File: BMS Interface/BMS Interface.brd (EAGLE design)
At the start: 55.2 x 82.9 mm, 23 parts

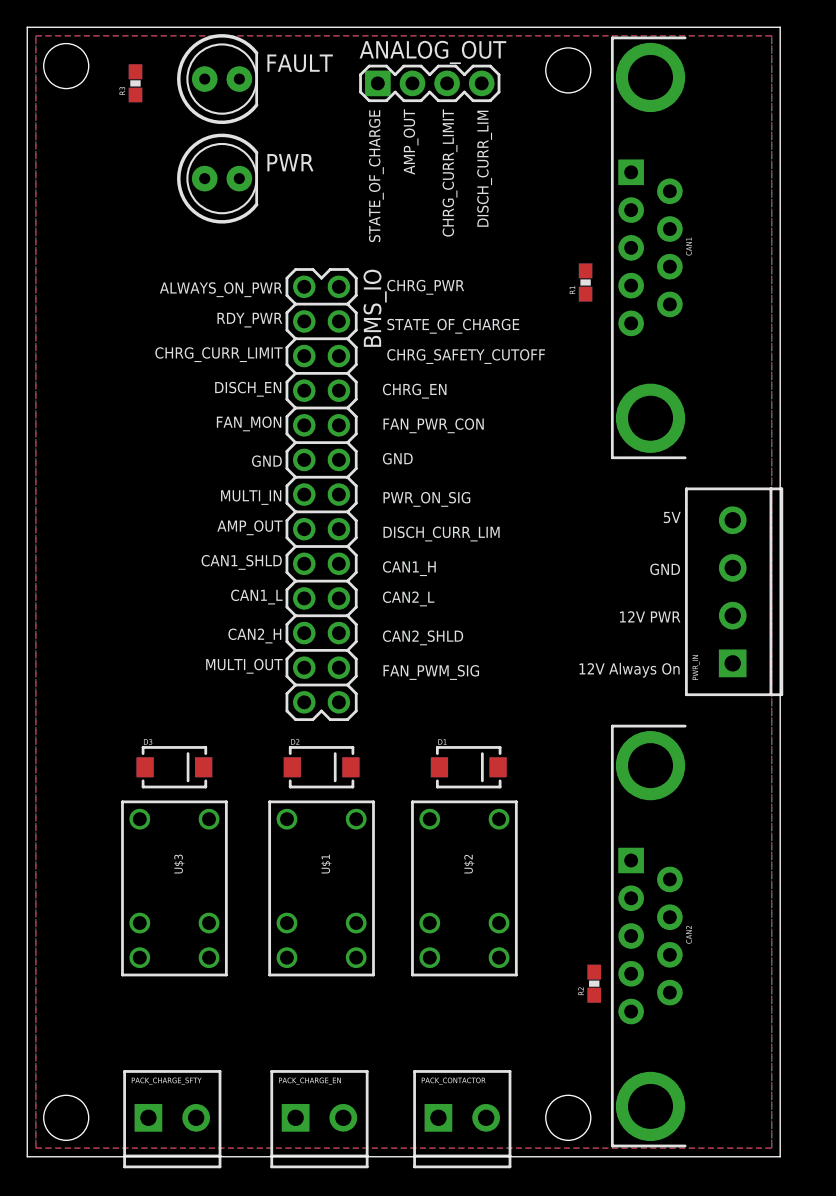
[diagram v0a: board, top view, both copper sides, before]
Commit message: Updating layout for BMS interface PCB and removed 5V input as it was no longer necessary.
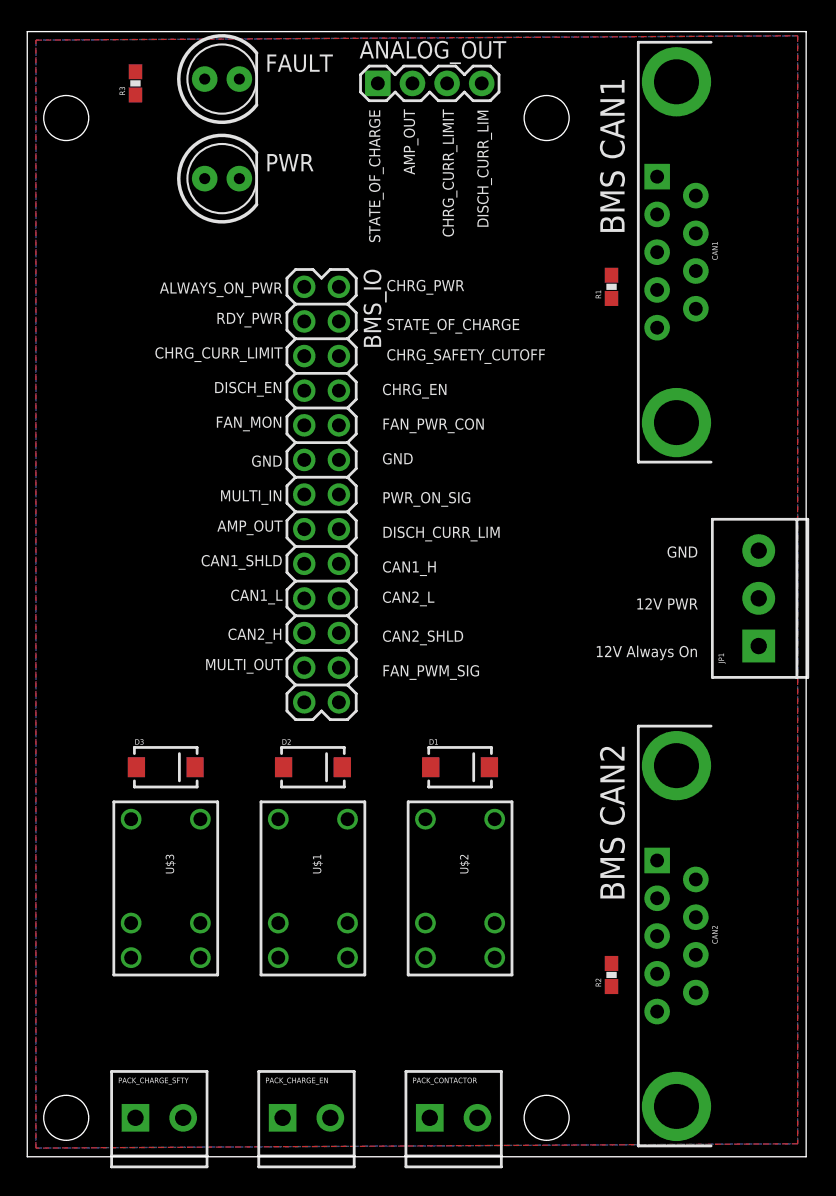
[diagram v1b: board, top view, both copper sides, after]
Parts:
- removed PWR_IN: (no value), SparkFun-Connectors:SCREWTERMINAL-3.5MM-4
- added JP1: (no value), SparkFun-Connectors:SCREWTERMINAL-3.5MM-3
- moved STANDOFF4 3.84 mm to (38.1, 76.2)
- moved STANDOFF2 3.81 mm to (2.86, 76.2)
- moved CAN1 1.93 mm to (47.6, 66.4)
- moved R1 1.93 mm to (42.9, 63.8)
- moved CAN2 1.91 mm to (47.6, 16.2)
- moved STANDOFF3 1.59 mm to (38.1, 2.86)
- moved R2 1.42 mm to (42.9, 13.3)
- moved PACK_CHARGE_SFTY 0.95 mm to (7.94, 2.86)
- moved PACK_CHARGE_EN 0.95 mm to (18.7, 2.86)
- moved D2 0.64 mm to (21.0, 28.6)
- moved PACK_CONTACTOR 0.64 mm to (29.5, 2.86)
- moved U$1 0.64 mm to (21.0, 19.7)
- moved D3 0.63 mm to (10.2, 28.6)
- moved U$3 0.63 mm to (10.2, 19.7)
- moved D1 0.63 mm to (31.8, 28.6)
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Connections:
- removed net 5V: PWR_IN.4
- net 12V_PWR: now also JP1.2; no longer PWR_IN.2
- net ALWAYS_ON_PWR: now also JP1.1; no longer PWR_IN.1
- net GND: now also JP1.3; no longer PWR_IN.3
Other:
- board size 55.2 x 82.9 mm -> 57.1 x 82.5 mm
- board text added: "BMS CAN1"
- board text added: "BMS CAN2"
- board text removed: "5V"

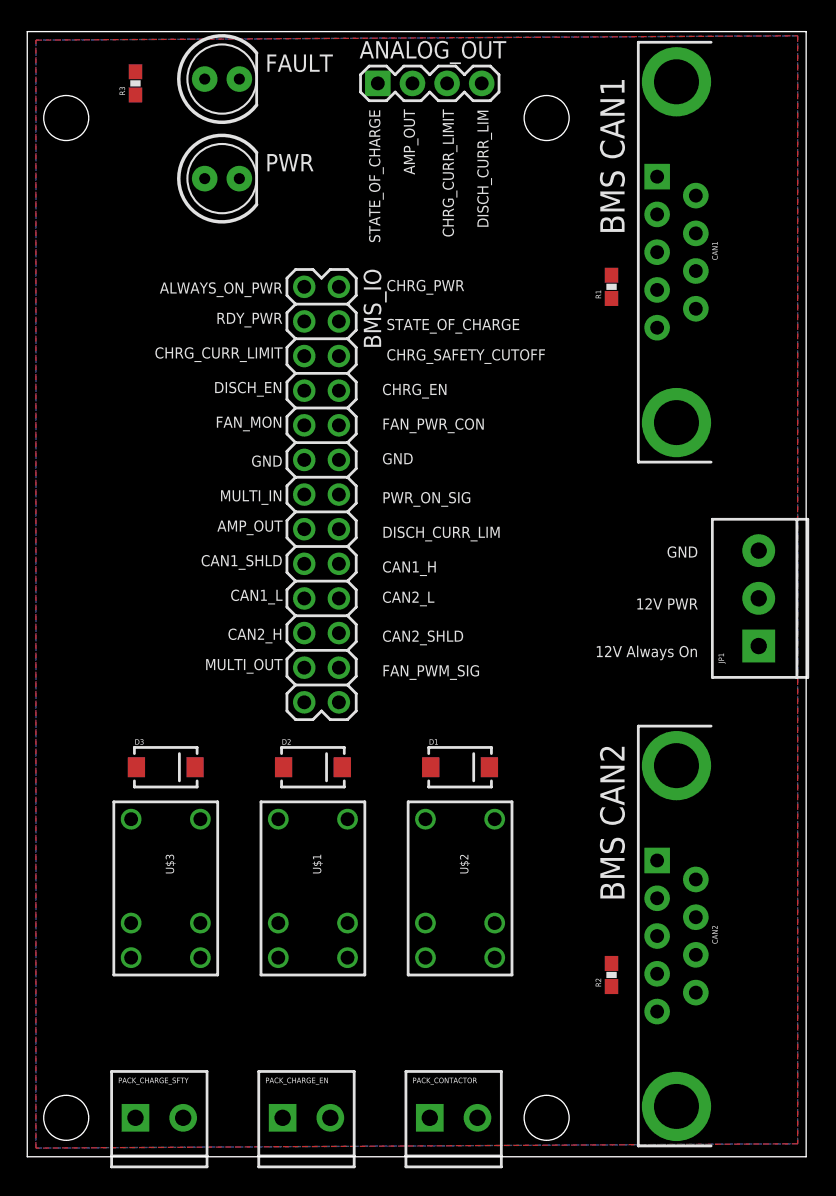
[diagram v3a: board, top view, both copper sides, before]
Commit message: CHanged all connectors on MCB to use Molex
Changed most of the connectors on the BMS interface to use molex as
well.
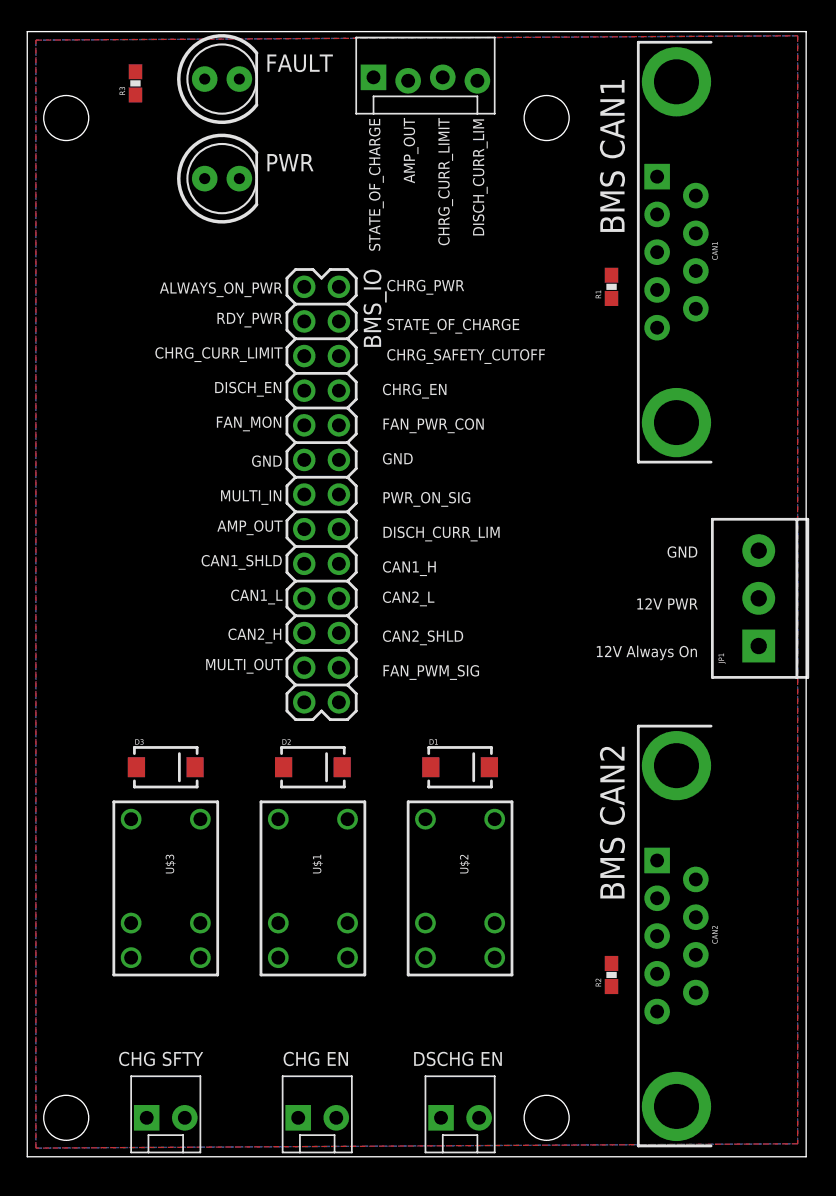
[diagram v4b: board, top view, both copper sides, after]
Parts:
- ANALOG_OUT: device SparkFun-Connectors:1X04 -> SparkFun-Connectors:MOLEX-1X4_LOCK
- PACK_CHARGE_EN, PACK_CHARGE_SFTY, PACK_CONTACTOR: value M023.5MM -> M02POLAR_LOCK; device SparkFun-Connectors:SCREWTERMINAL-3.5MM-2 -> SparkFun-Connectors:MOLEX-1X2_LOCK
- moved PACK_CHARGE_EN 1.27 mm to (20.0, 2.86)
- moved PACK_CHARGE_SFTY 0.95 mm to (8.89, 2.86)
- moved PACK_CONTACTOR 0.95 mm to (30.5, 2.86)
- moved ANALOG_OUT 0.45 mm to (25.4, 79.1)
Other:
- board text added: "CHG EN"
- board text added: "CHG SFTY"
- board text added: "DSCHG EN"
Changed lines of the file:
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@@
 <text x="49.2125" y="40.9575" size="0.8128" layer="25" font="vector" ratio="15" rot="R180">12V PWR</text>
 <text x="49.2125" y="44.7675" size="0.8128" layer="25" font="vector" ratio="15" rot="R180">GND</text>
-<text x="33.02" y="76.835" size="0.8128" layer="25" font="vector" ratio="15" rot="R270">DISCH_CURR_LIM</text>
-<text x="30.48" y="76.835" size="0.8128" layer="25" font="vector" ratio="15" rot="R270">CHRG_CURR_LIMIT</text>
-<text x="27.6225" y="76.835" size="0.8128" layer="25" font="vector" ratio="15" rot="R270">AMP_OUT</text>
-<text x="25.0825" y="76.835" size="0.8128" layer="25" font="vector" ratio="15" rot="R270">STATE_OF_CHARGE</text>
+<text x="32.7025" y="76.2" size="0.8128" layer="25" font="vector" ratio="15" rot="R270">DISCH_CURR_LIM</text>
+<text x="30.1625" y="76.2" size="0.8128" layer="25" font="vector" ratio="15" rot="R270">CHRG_CURR_LIMIT</text>
+<text x="27.6225" y="76.2" size="0.8128" layer="25" font="vector" ratio="15" rot="R270">AMP_OUT</text>
+<text x="25.0825" y="76.2" size="0.8128" layer="25" font="vector" ratio="15" rot="R270">STATE_OF_CHARGE</text>
 <text x="43.815" y="67.6275" size="1.778" layer="25" font="vector" ratio="15" rot="R90">BMS CAN1</text>
 <text x="43.815" y="18.7325" size="1.778" layer="25" font="vector" ratio="15" rot="R90">BMS CAN2</text>
+<text x="6.6675" y="6.6675" size="1.016" layer="25" font="vector" ratio="15">CHG SFTY</text>
+<text x="18.7325" y="6.6675" size="1.016" layer="25" font="vector" ratio="15">CHG EN</text>
+<text x="28.2575" y="6.6675" size="1.016" layer="25" font="vector" ratio="15">DSCHG EN</text>
 </plain>
 <attributes>
@@
 <element name="U$1" library="SparkFun-Electromechanical" package="RELAY-G5V" value="RELAY-2G5Q" x="20.955" y="19.685" rot="R270"/>
 <element name="U$2" library="SparkFun-Electromechanical" package="RELAY-G5V" value="RELAY-2G5Q" x="31.75" y="19.685" rot="R270"/>
-<element name="PACK_CONTACTOR" library="SparkFun-Connectors" package="SCREWTERMINAL-3.5MM-2" value="M023.5MM" x="29.5275" y="2.8575"/>
 <element name="D1" library="SparkFun-DiscreteSemi" package="SMA-DIODE" value="1n4001" x="31.75" y="28.575"/>
-<element name="PACK_CHARGE_EN" library="SparkFun-Connectors" package="SCREWTERMINAL-3.5MM-2" value="M023.5MM" x="18.7325" y="2.8575"/>
-<element name="PACK_CHARGE_SFTY" library="SparkFun-Connectors" package="SCREWTERMINAL-3.5MM-2" value="M023.5MM" x="7.9375" y="2.8575"/>
 <element name="D2" library="SparkFun-DiscreteSemi" package="SMA-DIODE" value="1n4001" x="20.955" y="28.575"/>
 <element name="U$3" library="SparkFun-Electromechanical" package="RELAY-G5V" value="RELAY-2G5Q" x="10.16" y="19.685" rot="R270"/>
@@
 <element name="FAULT" library="SparkFun-LED" package="LED5MM" value="Red" x="14.2875" y="79.0575"/>
 <element name="PWR" library="SparkFun-LED" package="LED5MM" value="GREEN" x="14.2875" y="71.755"/>
-<element name="ANALOG_OUT" library="SparkFun-Connectors" package="1X04" value="" x="25.7175" y="78.74"/>
 <element name="STANDOFF1" library="SparkFun-Electromechanical" package="STAND-OFF" value="STAND-OFF" x="2.8575" y="2.8575"/>
 <element name="STANDOFF2" library="SparkFun-Electromechanical" package="STAND-OFF" value="STAND-OFF" x="2.8575" y="76.2"/>
@@
 <element name="STANDOFF4" library="SparkFun-Electromechanical" package="STAND-OFF" value="STAND-OFF" x="38.1" y="76.2"/>
 <element name="JP1" library="SparkFun-Connectors" package="SCREWTERMINAL-3.5MM-3" value="" x="53.6575" y="37.465" rot="R90"/>
+<element name="ANALOG_OUT" library="SparkFun-Connectors" package="MOLEX-1X4_LOCK" value="" x="25.4" y="79.0575"/>
+<element name="PACK_CONTACTOR" library="SparkFun-Connectors" package="MOLEX-1X2_LOCK" value="M02POLAR_LOCK" x="30.48" y="2.8575"/>
+<element name="PACK_CHARGE_EN" library="SparkFun-Connectors" package="MOLEX-1X2_LOCK" value="M02POLAR_LOCK" x="20.0025" y="2.8575"/>
+<element name="PACK_CHARGE_SFTY" library="SparkFun-Connectors" package="MOLEX-1X2_LOCK" value="M02POLAR_LOCK" x="8.89" y="2.8575"/>
 </elements>
 <signals>
@@
 <contactref element="BMS_IO" pad="5"/>
 <contactref element="ANALOG_OUT" pad="3"/>
-<wire x1="20.32" y1="58.7375" x2="30.7975" y2="78.74" width="0" layer="19" extent="1-1"/>
+<wire x1="20.32" y1="58.7375" x2="30.48" y2="79.1845" width="0" layer="19" extent="1-1"/>
 </signal>
 <signal name="DISCHARGE_ENABLE">
@@
 <contactref element="BMS_IO" pad="11"/>
 <contactref element="BMS_IO" pad="12"/>
-<contactref element="PACK_CONTACTOR" pad="2"/>
-<contactref element="PACK_CHARGE_SFTY" pad="2"/>
 <contactref element="PWR" pad="K"/>
 <polygon width="0.254" layer="16" isolate="0.3048">
@@
 </polygon>
 <contactref element="JP1" pad="3"/>
+<contactref element="PACK_CONTACTOR" pad="2"/>
+<contactref element="PACK_CHARGE_SFTY" pad="2"/>
 </signal>
 <signal name="MULTIPURPOSE_INPUT">
@@
 <contactref element="BMS_IO" pad="15"/>
 <contactref element="ANALOG_OUT" pad="2"/>
-<wire x1="20.32" y1="46.0375" x2="28.2575" y2="78.74" width="0" layer="19" extent="1-1"/>
+<wire x1="20.32" y1="46.0375" x2="27.94" y2="78.9305" width="0" layer="19" extent="1-1"/>
 </signal>
 <signal name="CAN1_SHIELD">
@@
 <contactref element="BMS_IO" pad="4"/>
 <contactref element="ANALOG_OUT" pad="1"/>
-<wire x1="22.86" y1="61.2775" x2="25.7175" y2="78.74" width="0" layer="19" extent="1-1"/>
+<wire x1="22.86" y1="61.2775" x2="25.4" y2="79.1845" width="0" layer="19" extent="1-1"/>
 </signal>
 <signal name="CHARGE_SAFETY">
@@
 <contactref element="BMS_IO" pad="16"/>
 <contactref element="ANALOG_OUT" pad="4"/>
-<wire x1="22.86" y1="46.0375" x2="33.3375" y2="78.74" width="0" layer="19" extent="1-1"/>
+<wire x1="22.86" y1="46.0375" x2="33.02" y2="78.9305" width="0" layer="19" extent="1-1"/>
 </signal>
 <signal name="CAN1_H">
@@
 </signal>
 <signal name="PACK_CONTACT_OUT">
+<contactref element="U$2" pad="10"/>
 <contactref element="PACK_CONTACTOR" pad="1"/>
-<contactref element="U$2" pad="10"/>
-<wire x1="29.5275" y1="2.8575" x2="29.21" y2="14.605" width="0" layer="19" extent="1-1"/>
+<wire x1="30.353" y1="2.8575" x2="29.21" y2="14.605" width="0" layer="19" extent="1-1"/>
 </signal>
 <signal name="PACK_CHARGE_IN">
-<contactref element="PACK_CHARGE_EN" pad="1"/>
 <contactref element="U$1" pad="6"/>
 <contactref element="U$1" pad="5"/>
+<contactref element="PACK_CHARGE_EN" pad="1"/>
 <wire x1="18.415" y1="24.765" x2="23.495" y2="24.765" width="0" layer="19" extent="1-1"/>
-<wire x1="18.7325" y1="2.8575" x2="18.415" y2="24.765" width="0" layer="19" extent="1-1"/>
+<wire x1="19.8755" y1="2.8575" x2="18.415" y2="24.765" width="0" layer="19" extent="1-1"/>
 </signal>
 <signal name="PACK_CHARGE_OUT">
+<contactref element="U$1" pad="10"/>
 <contactref element="PACK_CHARGE_EN" pad="2"/>
-<contactref element="U$1" pad="10"/>
-<wire x1="22.2325" y1="2.8575" x2="18.415" y2="14.605" width="0" layer="19" extent="1-1"/>
+<wire x1="22.6695" y1="2.8575" x2="18.415" y2="14.605" width="0" layer="19" extent="1-1"/>
 </signal>
 <signal name="PACK_SAFETY_IN">
+<contactref element="U$3" pad="10"/>
 <contactref element="PACK_CHARGE_SFTY" pad="1"/>
-<contactref element="U$3" pad="10"/>
-<wire x1="7.9375" y1="2.8575" x2="7.62" y2="14.605" width="0" layer="19" extent="1-1"/>
+<wire x1="8.763" y1="2.8575" x2="7.62" y2="14.605" width="0" layer="19" extent="1-1"/>
 </signal>
 <signal name="N$2">
